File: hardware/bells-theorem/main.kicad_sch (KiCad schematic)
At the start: 6 parts, among them J2 left, J3 right, U1 Teensy4.1, U11 SN74LV1T34DBV, U3 MCP6002-xSN

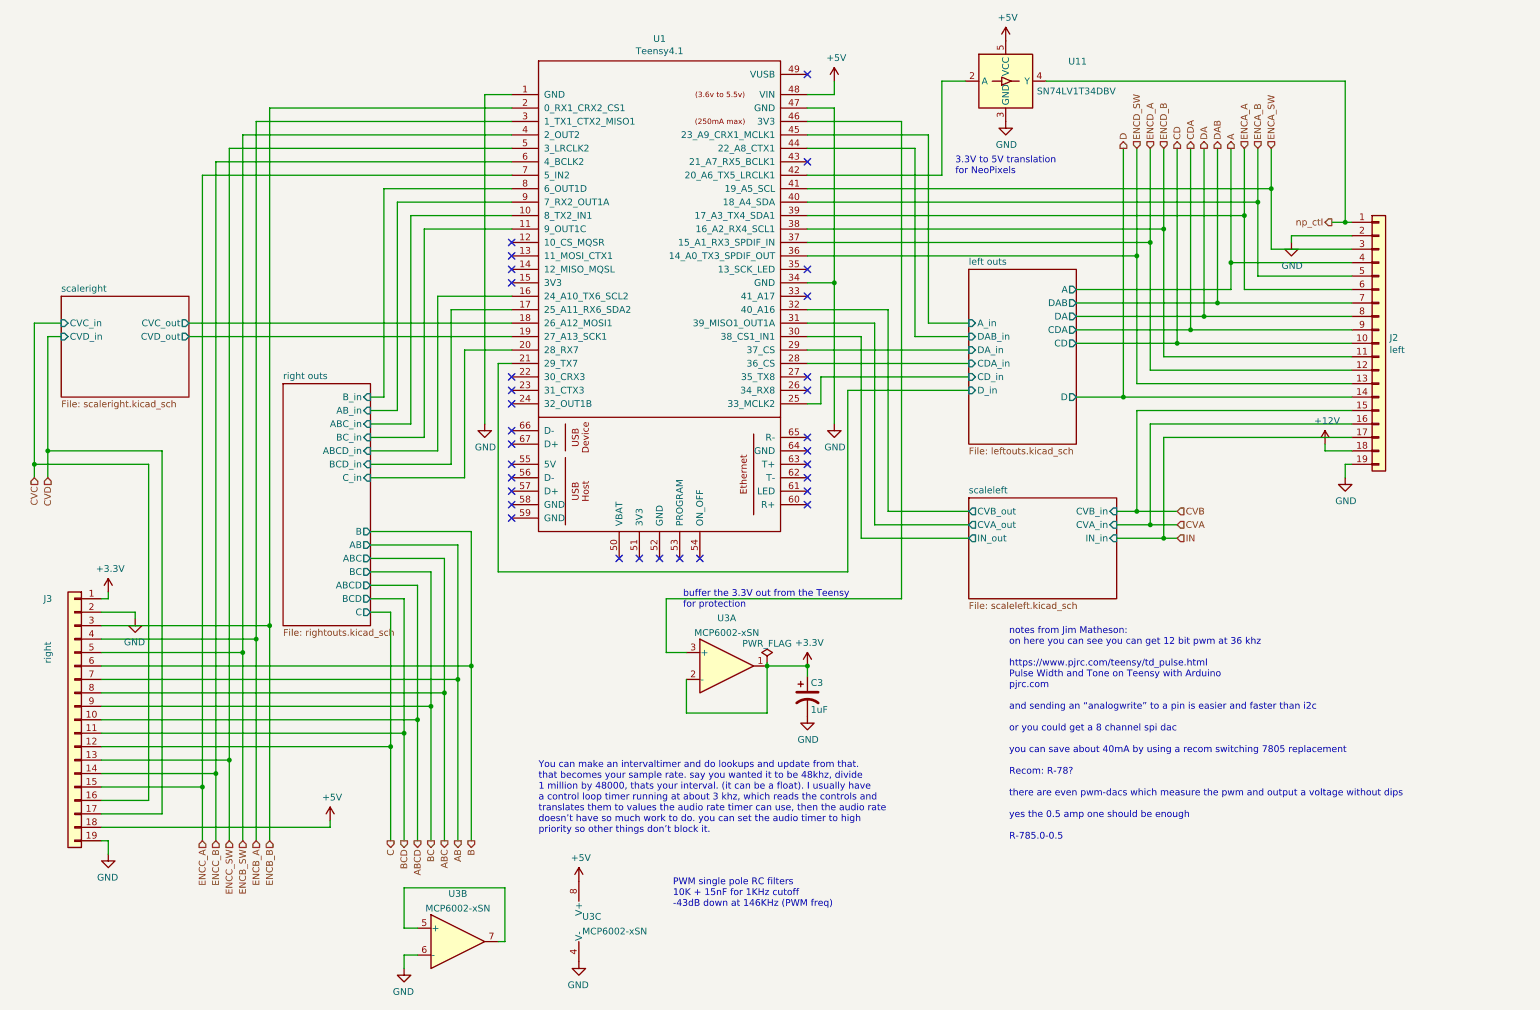
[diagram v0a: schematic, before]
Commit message: Modified with Jim M's recommendations for input scaling
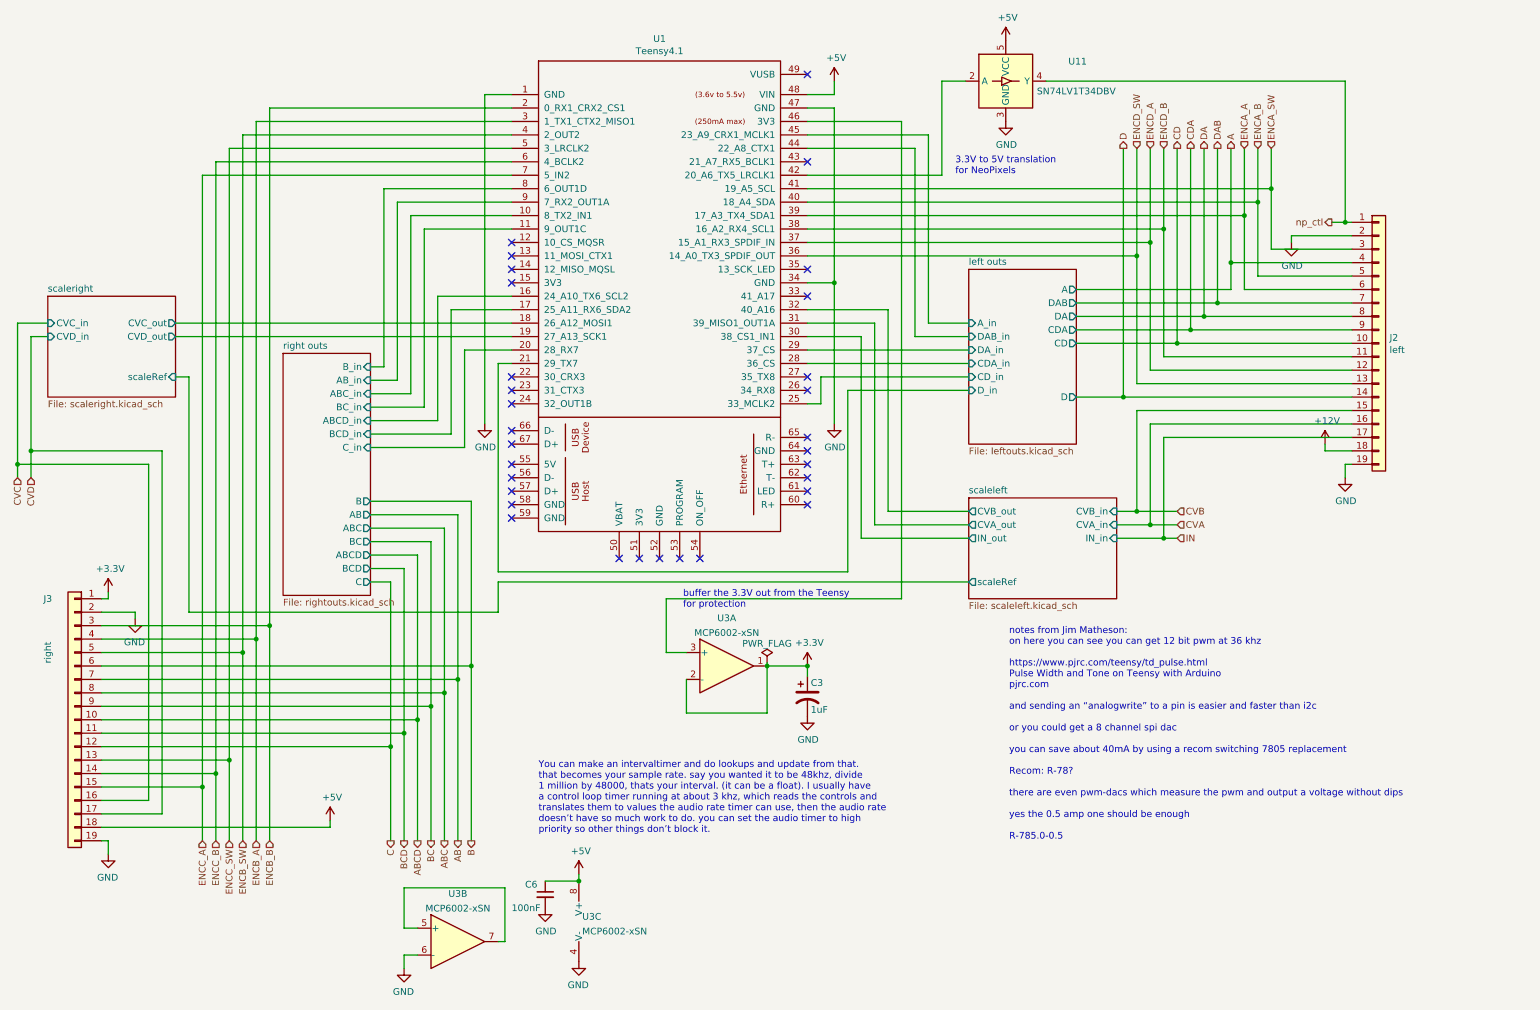
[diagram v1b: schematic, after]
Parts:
- added C6: 100nF, Capacitor_SMD:C_0805_2012Metric_Pad1.15x1.40mm_HandSolder, symbol Device:C_Small
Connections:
- net +5V: now also C6.1
- net GND: now also C6.2
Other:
- sheet scaleleft ports: added scaleRef; removed none
- sheet scaleright ports: added scaleRef; removed none
- note removed: "PWM single pole RC filters 10K + 15nF for 1KHz cutoff -43dB down at 146KHz (PWM freq)"

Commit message: All changes up to date with latest revisions
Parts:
- removed C3: 1uF, Capacitor_THT:CP_Radial_D5.0mm_P2.50mm, symbol Device:C_Polarized_US
- removed C6: 100nF, Capacitor_SMD:C_0805_2012Metric_Pad1.15x1.40mm_HandSolder, symbol Device:C_Small
- removed U3: MCP6002-xSN, Package_SO:SOIC-8_3.9x4.9mm_P1.27mm, symbol Amplifier_Operational:MCP6002-xSN
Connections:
- net 3Venable: now reaches U1.12 (10_CS_MQSR)
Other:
- note removed: "buffer the 3.3V out from the Teensy for protection"
- title: (none) -> Bell's Theorem

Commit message: last hardware / software updates
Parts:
- added C59, C60: 100nF, Capacitor_SMD:C_0805_2012Metric_Pad1.18x1.45mm_HandSolder, symbol Device:C_Small
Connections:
- net GND: now also C59.1, C60.2
- net at U1.15 (3V3): now also C59.2
- net at U1.46 (3V3): now also C60.1
- net +12V renamed +10V
- no-connect marks 31 -> 29
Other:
- sheet scaleleft ports: added none; removed scaleRef
- sheet scaleright ports: added none; removed scaleRef
- note added: "alternately can use SN74AHCT1G124DBVR but have to tie pin 1 to gnd"
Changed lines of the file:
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@@
   (junction (at 53.34 153.67) (diameter 0) (color 0 0 0 0)
   )
+  (junction (at 170.18 30.48) (diameter 0) (color 0 0 0 0)
+  )
   (junction (at 170.18 60.96) (diameter 0) (color 0 0 0 0)
+  )
+  (junction (at 104.14 60.96) (diameter 0) (color 0 0 0 0)
   )
   (junction (at 15.875 95.25) (diameter 0) (color 0 0 0 0)
@@
   (no_connect (at 109.22 81.28))
   (no_connect (at 165.1 92.71))
-  (no_connect (at 109.22 60.96))
   (no_connect (at 109.22 83.82))
   (no_connect (at 109.22 58.42))
@@
   (no_connect (at 165.1 21.59))
   (no_connect (at 165.1 63.5))
-  (no_connect (at 165.1 30.48))
   (no_connect (at 165.1 58.42))
   (no_connect (at 109.22 100.33))
@@
     (stroke (width 0) (type default) (color 0 0 0 0))
   )
-  (wire (pts (xy 175.26 117.475) (xy 175.26 123.19))
-    (stroke (width 0) (type default) (color 0 0 0 0))
-  )
   (wire (pts (xy 252.73 43.18) (xy 165.1 43.18))
     (stroke (width 0) (type default) (color 0 0 0 0))
@@
     (stroke (width 0) (type default) (color 0 0 0 0))
   )
-  (wire (pts (xy 48.26 78.74) (xy 45.72 78.74))
-    (stroke (width 0) (type default) (color 0 0 0 0))
-  )
   (wire (pts (xy 109.22 38.1) (xy 53.34 38.1))
     (stroke (width 0) (type default) (color 0 0 0 0))
@@
     (stroke (width 0) (type default) (color 0 0 0 0))
   )
+  (wire (pts (xy 170.18 30.48) (xy 170.18 27.94))
+    (stroke (width 0) (type default) (color 0 0 0 0))
+  )
   (wire (pts (xy 31.75 130.81) (xy 58.42 130.81))
     (stroke (width 0) (type default) (color 0 0 0 0))
@@
     (stroke (width 0) (type default) (color 0 0 0 0))
   )
-  (wire (pts (xy 104.14 25.4) (xy 104.14 87.63))
+  (wire (pts (xy 104.14 25.4) (xy 104.14 60.96))
     (stroke (width 0) (type default) (color 0 0 0 0))
   )
@@
     (stroke (width 0) (type default) (color 0 0 0 0))
   )
-  (wire (pts (xy 48.26 123.19) (xy 48.26 78.74))
-    (stroke (width 0) (type default) (color 0 0 0 0))
-  )
   (wire (pts (xy 180.34 66.04) (xy 180.34 104.14))
     (stroke (width 0) (type default) (color 0 0 0 0))
@@
     (stroke (width 0) (type default) (color 0 0 0 0))
   )
+  (wire (pts (xy 104.14 60.96) (xy 104.14 87.63))
+    (stroke (width 0) (type default) (color 0 0 0 0))
+  )
   (wire (pts (xy 86.36 148.59) (xy 31.75 148.59))
     (stroke (width 0) (type default) (color 0 0 0 0))
@@
     (stroke (width 0) (type default) (color 0 0 0 0))
   )
-  (wire (pts (xy 170.18 60.96) (xy 170.18 27.94))
+  (wire (pts (xy 170.18 60.96) (xy 170.18 30.48))
     (stroke (width 0) (type default) (color 0 0 0 0))
   )
@@
     (stroke (width 0) (type default) (color 0 0 0 0))
   )
-  (wire (pts (xy 175.26 123.19) (xy 48.26 123.19))
-    (stroke (width 0) (type default) (color 0 0 0 0))
-  )
   (wire (pts (xy 185.42 35.56) (xy 185.42 71.12))
     (stroke (width 0) (type default) (color 0 0 0 0))
@@
     (stroke (width 0) (type default) (color 0 0 0 0))
   )
-  (wire (pts (xy 195.58 117.475) (xy 175.26 117.475))
-    (stroke (width 0) (type default) (color 0 0 0 0))
-  )
   (wire (pts (xy 187.96 33.02) (xy 187.96 68.58))
     (stroke (width 0) (type default) (color 0 0 0 0))
@@
   )
   (text "You can make an intervaltimer and do lookups and update from that. \nthat becomes your sample rate. say you wanted it to be 48khz, divide \n1 million by 48000, thats your interval. (it can be a float). I usually have \na control loop timer running at about 3 khz, which reads the controls and\ntranslates them to values the audio rate timer can use, then the audio rate\ndoesn’t have so much work to do. you can set the audio timer to high \npriority so other things don’t block it."
-    (at 114.3 165.1 0)
+    (at 114.3 144.78 0)
     (effects (font (size 1.27 1.27)) (justify left bottom))
   )
@@
     (effects (font (size 1.27 1.27)) (justify left bottom))
   )
-  (text "3.3V to 5V translation\nfor NeoPixels" (at 193.04 40.64 0)
+  (text "3.3V to 5V translation\nfor NeoPixels" (at 177.8 19.05 0)
+    (effects (font (size 1.27 1.27)) (justify left bottom))
+  )
+  (text "alternately can use\nSN74AHCT1G124DBVR\nbut have to tie pin 1 to gnd"
+    (at 193.04 41.91 0)
     (effects (font (size 1.27 1.27)) (justify left bottom))
   )
@@
     (pin "1")
   )
-  (symbol (lib_id "power:+12V") (at 262.89 91.44 0) (unit 1)
-    (in_bom yes) (on_board yes)
-    (property "Reference" "#PWR05" (id 0) (at 262.89 95.25 0)
-      (effects (font (size 1.27 1.27)) hide)
-    )
-    (property "Value" "+12V" (id 1) (at 263.271 87.0458 0))
-    (property "Footprint" "" (id 2) (at 262.89 91.44 0)
-      (effects (font (size 1.27 1.27)) hide)
-    )
-    (property "Datasheet" "" (id 3) (at 262.89 91.44 0)
-      (effects (font (size 1.27 1.27)) hide)
-    )
-    (pin "1")
-  )
   (symbol (lib_id "power:+3.3V") (at 33.02 119.38 0) (unit 1)
     (in_bom yes) (on_board yes)
@@
     (pin "1")
   )
+  (symbol (lib_id "Device:C_Small") (at 106.68 60.96 90) (unit 1)
+    (in_bom yes) (on_board yes)
+    (property "Reference" "C59" (id 0) (at 101.6 60.325 90))
+    (property "Value" "100nF" (id 1) (at 100.33 62.23 90))
+    (property "Footprint" "Capacitor_SMD:C_0805_2012Metric_Pad1.18x1.45mm_HandSolder" (id 2) (at 106.68 60.96 0)
+      (effects (font (size 1.27 1.27)) hide)
+    )
+    (property "Datasheet" "~" (id 3) (at 106.68 60.96 0)
+      (effects (font (size 1.27 1.27)) hide)
+    )
+    (pin "1")
+    (pin "2")
+  )
   (symbol (lib_id "Logic_LevelTranslator:SN74LV1T34DBV") (at 202.565 22.86 0) (unit 1)
     (in_bom yes) (on_board yes)
@@
     (pin "4")
     (pin "5")
+  )
+  (symbol (lib_id "power:+10V") (at 262.89 91.44 0) (unit 1)
+    (in_bom yes) (on_board yes) (fields_autoplaced)
+    (property "Reference" "#PWR?" (id 0) (at 262.89 95.25 0)
+      (effects (font (size 1.27 1.27)) hide)
+    )
+    (property "Value" "+10V" (id 1) (at 262.89 87.8355 0))
+    (property "Footprint" "" (id 2) (at 262.89 91.44 0)
+      (effects (font (size 1.27 1.27)) hide)
+    )
+    (property "Datasheet" "" (id 3) (at 262.89 91.44 0)
+      (effects (font (size 1.27 1.27)) hide)
+    )
+    (pin "1")
+  )
+  (symbol (lib_id "Device:C_Small") (at 167.64 30.48 90) (unit 1)
+    (in_bom yes) (on_board yes)
+    (property "Reference" "C60" (id 0) (at 172.085 29.21 90))
+    (property "Value" "100nF" (id 1) (at 173.99 31.115 90))
+    (property "Footprint" "Capacitor_SMD:C_0805_2012Metric_Pad1.18x1.45mm_HandSolder" (id 2) (at 167.64 30.48 0)
+      (effects (font (size 1.27 1.27)) hide)
+    )
+    (property "Datasheet" "~" (id 3) (at 167.64 30.48 0)
+      (effects (font (size 1.27 1.27)) hide)
+    )
+    (pin "1")
+    (pin "2")
   )
   (sheet (at 21.59 63.5) (size 24.13 19.05) (fields_autoplaced)
@@
       (effects (font (size 1.27 1.27)) (justify left))
     )
-    (pin "scaleRef" input (at 45.72 78.74 0)
-      (effects (font (size 1.27 1.27)) (justify right))
-    )
   )
   (sheet (at 195.58 101.6) (size 27.94 19.05) (fields_autoplaced)
@@
       (effects (font (size 1.27 1.27)) (justify left))
     )
-    (pin "scaleRef" output (at 195.58 117.475 180)
-      (effects (font (size 1.27 1.27)) (justify left))
-    )

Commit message: checking in old outstanding changes prior to debugging with Claude Code
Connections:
- net +10V is gone; now on net +5V: J2.18 (Pin_18)
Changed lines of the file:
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@@
+    (stroke (width 0) (type default) (color 0 0 0 0))
+  )
+  (wire (pts (xy 261.62 92.71) (xy 267.97 92.71))
     (stroke (width 0) (type default) (color 0 0 0 0))
   )
@@
     (stroke (width 0) (type default) (color 0 0 0 0))
   )
-  (wire (pts (xy 262.89 92.71) (xy 267.97 92.71))
-    (stroke (width 0) (type default) (color 0 0 0 0))
-  )
   (wire (pts (xy 43.18 92.71) (xy 18.415 92.71))
     (stroke (width 0) (type default) (color 0 0 0 0))
@@
     (stroke (width 0) (type default) (color 0 0 0 0))
   )
-  (wire (pts (xy 262.89 91.44) (xy 262.89 92.71))
-    (stroke (width 0) (type default) (color 0 0 0 0))
-  )
   (wire (pts (xy 109.22 40.64) (xy 50.8 40.64))
     (stroke (width 0) (type default) (color 0 0 0 0))
@@
   )
   (wire (pts (xy 101.6 166.37) (xy 101.6 133.35))
+    (stroke (width 0) (type default) (color 0 0 0 0))
+  )
+  (wire (pts (xy 261.62 91.44) (xy 261.62 92.71))
     (stroke (width 0) (type default) (color 0 0 0 0))
   )
@@
     (pin "2")
   )
+  (symbol (lib_id "power:+5V") (at 261.62 91.44 0) (unit 1)
+    (in_bom yes) (on_board yes)
+    (property "Reference" "#PWR0128" (id 0) (at 261.62 95.25 0)
+      (effects (font (size 1.27 1.27)) hide)
+    )
+    (property "Value" "+5V" (id 1) (at 262.001 87.0458 0))
+    (property "Footprint" "" (id 2) (at 261.62 91.44 0)
+      (effects (font (size 1.27 1.27)) hide)
+    )
+    (property "Datasheet" "" (id 3) (at 261.62 91.44 0)
+      (effects (font (size 1.27 1.27)) hide)
+    )
+    (pin "1")
+  )
   (symbol (lib_id "Logic_LevelTranslator:SN74LV1T34DBV") (at 202.565 22.86 0) (unit 1)
     (in_bom yes) (on_board yes)
@@
     (pin "5")
   )
-  (symbol (lib_id "power:+10V") (at 262.89 91.44 0) (unit 1)
-    (in_bom yes) (on_board yes) (fields_autoplaced)
-    (property "Reference" "#PWR035" (id 0) (at 262.89 95.25 0)
-      (effects (font (size 1.27 1.27)) hide)
-    )
-    (property "Value" "+10V" (id 1) (at 262.89 87.8355 0))
-    (property "Footprint" "" (id 2) (at 262.89 91.44 0)
-      (effects (font (size 1.27 1.27)) hide)
-    )
-    (property "Datasheet" "" (id 3) (at 262.89 91.44 0)
-      (effects (font (size 1.27 1.27)) hide)
-    )
-    (pin "1")
-  )
   (symbol (lib_id "Device:C_Small") (at 167.64 30.48 90) (unit 1)
